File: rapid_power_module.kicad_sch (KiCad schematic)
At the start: 198 parts, among them J1 Conn_02x04_Top_Bottom, J11 SWD Header, J12 SWD Header, J16 USB_C_Receptacle_USB2.0, J17 TC2050, J2 Conn_02x03_Odd_Even, J3 Conn_02x04_Top_Bottom, J4 Conn_02x03_Odd_Even, J5 Molex MicroFit 2x2, J6 Molex MicroFit 2x2, J7 Molex MicroFit 2x2, J8 Molex MicroFit 2x2, J9 Molex MicroFit 2x2, Q1 Q_PMOS, Q2 Q_PMOS, Q3 Q_PMOS, Q4 Q_PMOS, Q5 NMOS, Q6 NMOS, Q7 NMOS, Q8 NMOS, SW1 KMR721NGLFS, SW2 KMR721NGLFS, U1 BQ25756RRVR, U10 L7805, U11 MCP2562-E-SN, U12 STM32F105RCTx, U13 AZ1117I-3.3, U14 TPD4E1U06, U15 TPD4E1U06, U2 CYPD3177-24LQ, U3 BQ76952PFBR, Y3 8MHz 12pF

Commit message: Added Footprints for MOSFETs
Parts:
- J2, J4: footprint (none) -> Connector_PinHeader_2.54mm:PinHeader_2x03_P2.54mm_Vertical
- Q1, Q2, Q3, Q4: footprint (none) -> Package_SO:Diodes_SO-8EP; LCSC (none) -> C531177
- Q5, Q6, Q7, Q8: footprint Package_DFN_QFN:AO_DFN-8-1EP_5.55x5.2mm_P1.27mm_EP4.12x4.6mm -> Package_SON:Infineon_PG-TDSON-8_6.15x5.15mm; LCSC C20266282 -> C501503
- R1: footprint (none) -> Resistor_SMD:R_0402_1005Metric
- TP1: footprint (none) -> TestPoint:TestPoint_Pad_D1.0mm
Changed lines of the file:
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@@
 			)
 		)
-		(property "Footprint" ""
+		(property "Footprint" "Connector_PinHeader_2.54mm:PinHeader_2x03_P2.54mm_Vertical"
 			(at 198.12 161.29 0)
 			(effects
@@
 			)
 		)
-		(property "Footprint" ""
+		(property "Footprint" "Resistor_SMD:R_0402_1005Metric"
 			(at 52.578 54.61 90)
 			(effects
@@
 			)
 		)
-		(property "Footprint" ""
+		(property "Footprint" "Package_SO:Diodes_SO-8EP"
 			(at 349.25 246.38 0)
 			(effects
@@
 			)
 		)
+		(property "LCSC" "C531177"
+			(at 351.79 251.46 90)
+			(effects
+				(font
+					(size 1.27 1.27)
+				)
+				(hide yes)
+			)
+		)
 		(pin "D"
 		)
@@
 			)
 		)
-		(property "Footprint" "Package_DFN_QFN:AO_DFN-8-1EP_5.55x5.2mm_P1.27mm_EP4.12x4.6mm"
+		(property "Footprint" "Package_SON:Infineon_PG-TDSON-8_6.15x5.15mm"
 			(at 134.62 81.28 0)
 			(effects
@@
 			)
 		)
-		(property "LCSC" "C20266282"
+		(property "LCSC" "C501503"
 			(at 139.7 83.82 0)
 			(effects
@@
 			)
 		)
-		(property "Footprint" ""
+		(property "Footprint" "TestPoint:TestPoint_Pad_D1.0mm"
 			(at 283.21 71.12 0)
 			(effects
@@
 			)
 		)
-		(property "Footprint" ""
+		(property "Footprint" "Package_SO:Diodes_SO-8EP"
 			(at 383.54 273.05 0)
 			(effects
@@
 			)
 		)
+		(property "LCSC" "C531177"
+			(at 381 278.13 90)
+			(effects
+				(font
+					(size 1.27 1.27)
+				)
+				(hide yes)
+			)
+		)
 		(pin "S"
 		)
@@
 			)
 		)
-		(property "Footprint" "Package_DFN_QFN:AO_DFN-8-1EP_5.55x5.2mm_P1.27mm_EP4.12x4.6mm"
+		(property "Footprint" "Package_SON:Infineon_PG-TDSON-8_6.15x5.15mm"
 			(at 119.38 81.28 0)
 			(effects
@@
 			)
 		)
-		(property "LCSC" "C20266282"
+		(property "LCSC" "C501503"
 			(at 114.3 83.82 0)
 			(effects
@@
 			)
 		)
-		(property "Footprint" ""
+		(property "Footprint" "Package_SO:Diodes_SO-8EP"
 			(at 349.25 273.05 0)
 			(effects
@@
 			)
 		)
+		(property "LCSC" "C531177"
+			(at 351.79 278.13 90)
+			(effects
+				(font
+					(size 1.27 1.27)
+				)
+				(hide yes)
+			)
+		)
 		(pin "D"
 		)
@@
 			)
 		)
-		(property "Footprint" "Package_DFN_QFN:AO_DFN-8-1EP_5.55x5.2mm_P1.27mm_EP4.12x4.6mm"
+		(property "Footprint" "Package_SON:Infineon_PG-TDSON-8_6.15x5.15mm"
 			(at 134.62 92.71 0)
 			(effects
@@
 			)
 		)
-		(property "LCSC" "C20266282"
+		(property "LCSC" "C501503"
 			(at 139.7 95.25 0)
 			(effects
@@
 			)
 		)
-		(property "Footprint" "Package_DFN_QFN:AO_DFN-8-1EP_5.55x5.2mm_P1.27mm_EP4.12x4.6mm"
+		(property "Footprint" "Package_SON:Infineon_PG-TDSON-8_6.15x5.15mm"
 			(at 119.38 92.71 0)
 			(effects
@@
 			)
 		)
-		(property "LCSC" "C20266282"
+		(property "LCSC" "C501503"
 			(at 114.3 95.25 0)
 			(effects
@@
 			)
 		)
-		(property "Footprint" ""
+		(property "Footprint" "Package_SO:Diodes_SO-8EP"
 			(at 383.54 246.38 0)
 			(effects
@@
 			)
 		)
+		(property "LCSC" "C531177"
+			(at 381 251.46 90)
+			(effects
+				(font
+					(size 1.27 1.27)
+				)
+				(hide yes)
+			)
+		)
 		(pin "S"
 		)
@@
 			)
 		)
-		(property "Footprint" ""
+		(property "Footprint" "Connector_PinHeader_2.54mm:PinHeader_2x03_P2.54mm_Vertical"
 			(at 179.07 161.29 0)
 			(effects

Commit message: Further Routing work and fixed the Q Pins
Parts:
- removed Q1, Q2, Q3, Q4: Q_PMOS, Package_SO:Diodes_SO-8EP, symbol Device:Q_PMOS
- added Q1, Q12, Q2, Q3: AOSP21321, Package_SO:SO-8_3.9x4.9mm_P1.27mm, symbol euroc_fc:AOSP21321
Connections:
- net SAFE_PWR_OUT: now also Q3.1 (S), Q3.2 (S), Q3.3 (S)
- net USB_PD_OUT: now also Q1.1 (S), Q1.2 (S), Q1.3 (S)
- net VBUS: now also Q12.5 (D), Q12.6 (D), Q12.7 (D), Q12.8 (D), Q2.5 (D), Q2.6 (D), Q2.7 (D), Q2.8 (D)
- net at C10.2, C9.2, R4.2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: now also Q1.4 (G), Q12.4 (G)
- net at R8.2, R9.1: now also Q2.4 (G), Q3.4 (G)
- new net: Q1.5 (D), Q1.6 (D), Q1.7 (D), Q1.8 (D), Q12.1 (S), Q12.2 (S), Q12.3 (S)
- new net: Q2.1 (S), Q2.2 (S), Q2.3 (S), Q3.5 (D), Q3.6 (D), Q3.7 (D), Q3.8 (D)

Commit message: Further Routing work and fixed the Q Pins
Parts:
- removed Q5, Q6, Q7, Q8: NMOS, Package_SON:Infineon_PG-TDSON-8_6.15x5.15mm, symbol Simulation_SPICE:NMOS
- added Q4: HiDRV1, Package_TO_SOT_SMD:TDSON-8-1, symbol Transistor_FET:BSC070N10NS5
- added Q5: LoDRV1, Package_TO_SOT_SMD:TDSON-8-1, symbol Transistor_FET:BSC070N10NS5
- added Q6: HiDRV2, Package_TO_SOT_SMD:TDSON-8-1, symbol Transistor_FET:BSC070N10NS5
- added Q7: LoDRV2, Package_TO_SOT_SMD:TDSON-8-1, symbol Transistor_FET:BSC070N10NS5
- added R25: 20k, Resistor_SMD:R_0402_1005Metric, symbol Device:R
- added R27: 50k, Resistor_SMD:R_0402_1005Metric, symbol Device:R
- R83: footprint Resistor_SMD:R_0603_1608Metric -> Resistor_SMD:R_0402_1005Metric; LCSC (none) -> C23184
- R94: value 16k -> 20k; footprint Resistor_SMD:R_0603_1608Metric -> Resistor_SMD:R_0402_1005Metric; LCSC (none) -> C25765
- R95: value 8k -> 10k; footprint Resistor_SMD:R_0603_1608Metric -> Resistor_SMD:R_0402_1005Metric; LCSC (none) -> C25744
- R96: value 4k -> 5.1k; footprint Resistor_SMD:R_0603_1608Metric -> Resistor_SMD:R_0402_1005Metric; LCSC (none) -> C25905
- R97: footprint Resistor_SMD:R_0603_1608Metric -> Resistor_SMD:R_0402_1005Metric; LCSC (none) -> C25765
- R98: value 12.5k -> 15k; LCSC (none) -> C25756
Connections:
- net BuckBoostOut: now also Q6.5 (D)
- net HIDRV1: now also Q4.4 (G)
- net HIDRV2: now also Q6.4 (G)
- net LODRV1: now also Q5.4 (G)
- net LODRV2: now also Q7.4 (G)
- net PACK+: now also BT1.P (+); no longer BT1.1 (+)
- net PGND: now also BT3.N (-), Q5.1 (S), Q5.2 (S), Q5.3 (S), Q7.1 (S), Q7.2 (S), Q7.3 (S), R25.2, R27.2; no longer BT3.2 (-)
- net SW1: now also Q4.1 (S), Q4.2 (S), Q4.3 (S), Q5.5 (D)
- net SW2: now also Q6.1 (S), Q6.2 (S), Q6.3 (S), Q7.5 (D)
- net at J4.1 (Pin_1): now also R27.1
- net at C4.1, C7.1, R65.2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: now also Q4.5 (D)
- net at J2.1 (Pin_1): now also R25.1
- new net: BT2.N (-), BT3.P (+), R12.1
- new net: BT1.N (-), BT2.P (+), R11.1
- no-connect marks 40 -> 38
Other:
- note removed: "TODO: Set Values"
- moved on the sheet: J2, J4, R32, R36, R82, R94, R95, R96, R97, R98, TH1

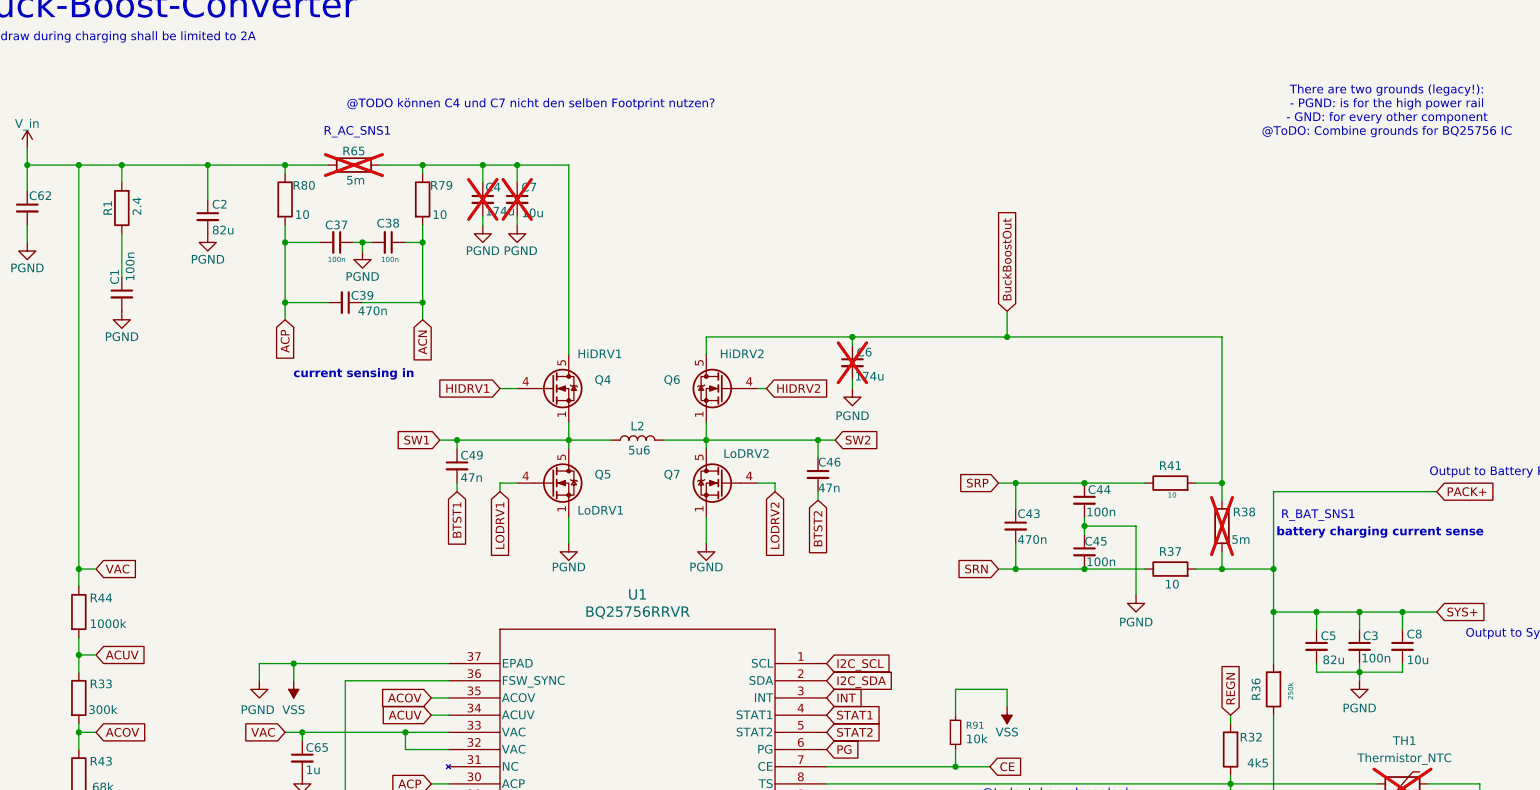
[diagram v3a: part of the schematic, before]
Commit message: Fixed wuerth cap footprints and values
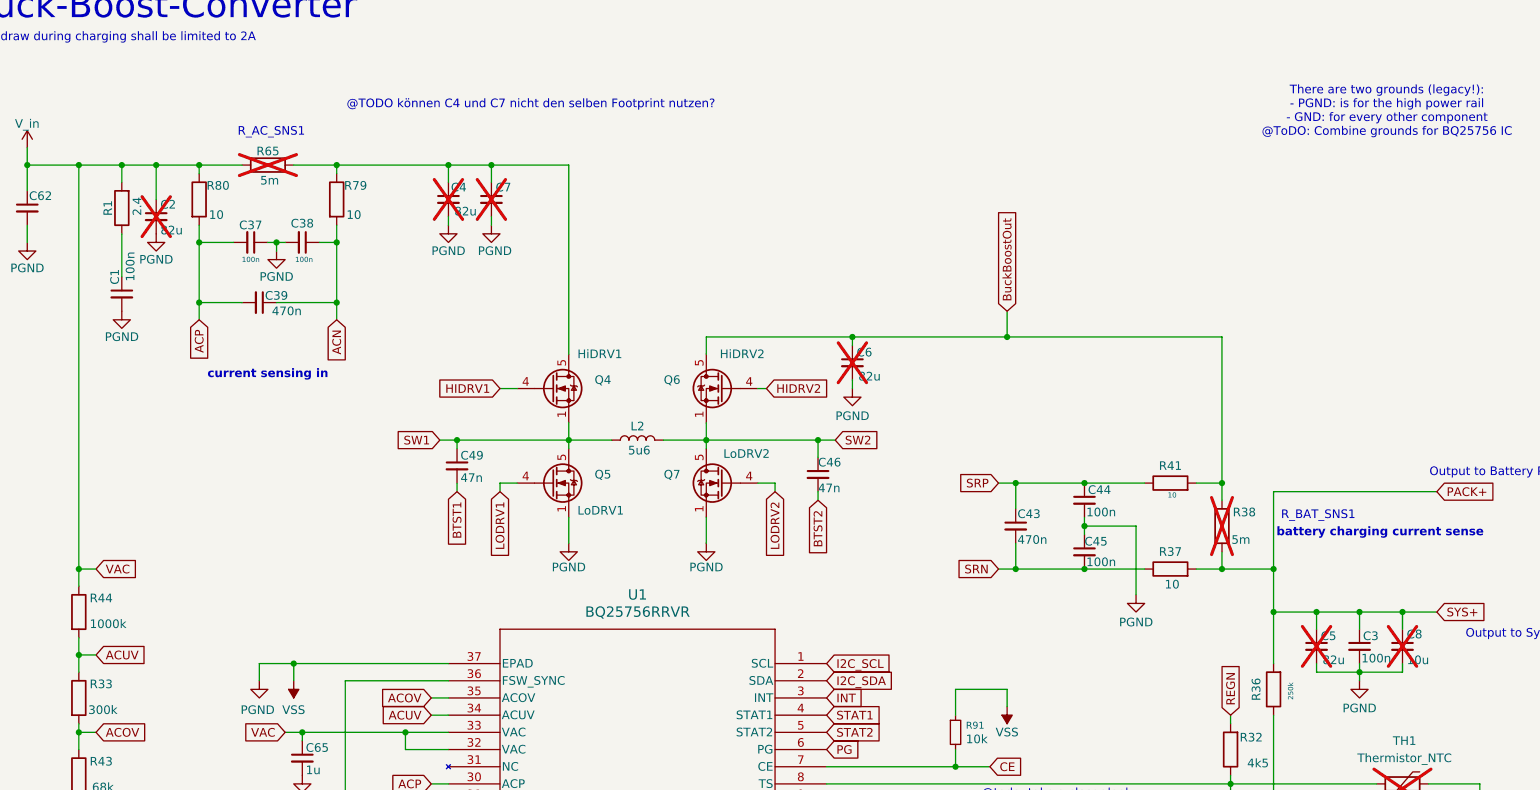
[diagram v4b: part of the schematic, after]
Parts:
- C2, C5: footprint Capacitor_SMD:C_0603_1608Metric -> Capacitor_SMD:CP_Elec_8x6.9; now not fitted
- C4, C6: value 174u -> 82u
- C8: footprint Capacitor_SMD:C_0603_1608Metric -> Capacitor_SMD:CP_Elec_6.3x5.9; now not fitted
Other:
- moved on the sheet: C37, C38, C39, C4, C7, R65, R79, R80

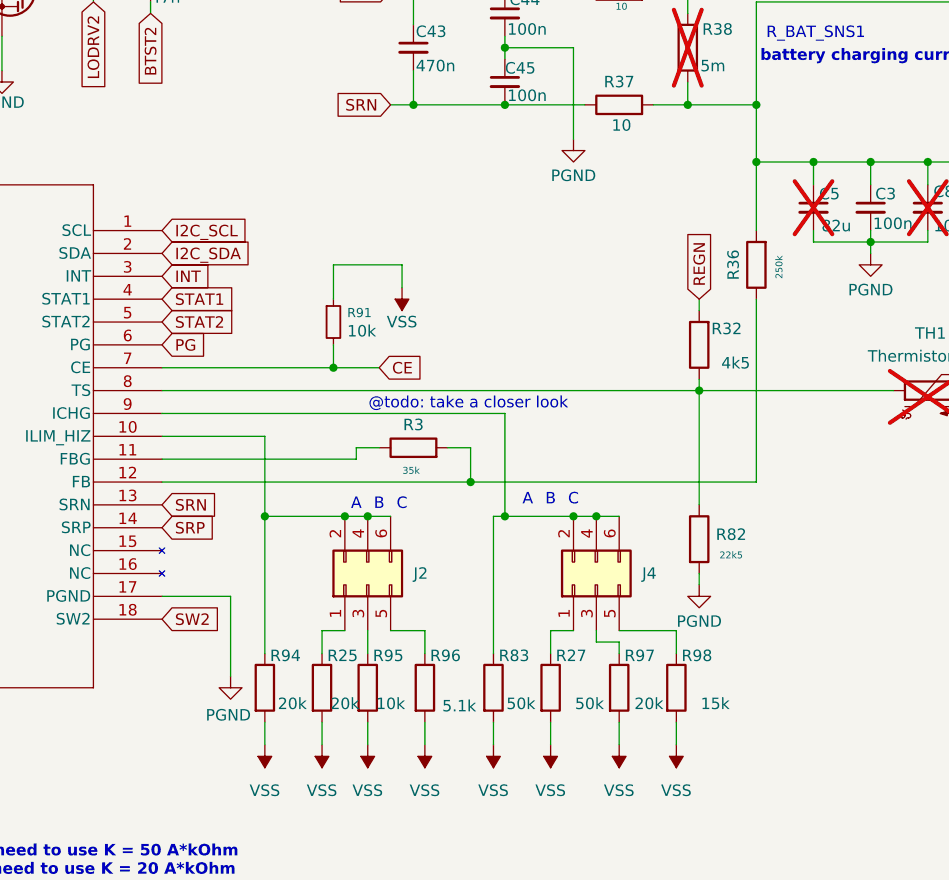
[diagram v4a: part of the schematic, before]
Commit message: Added footprints and LCSC
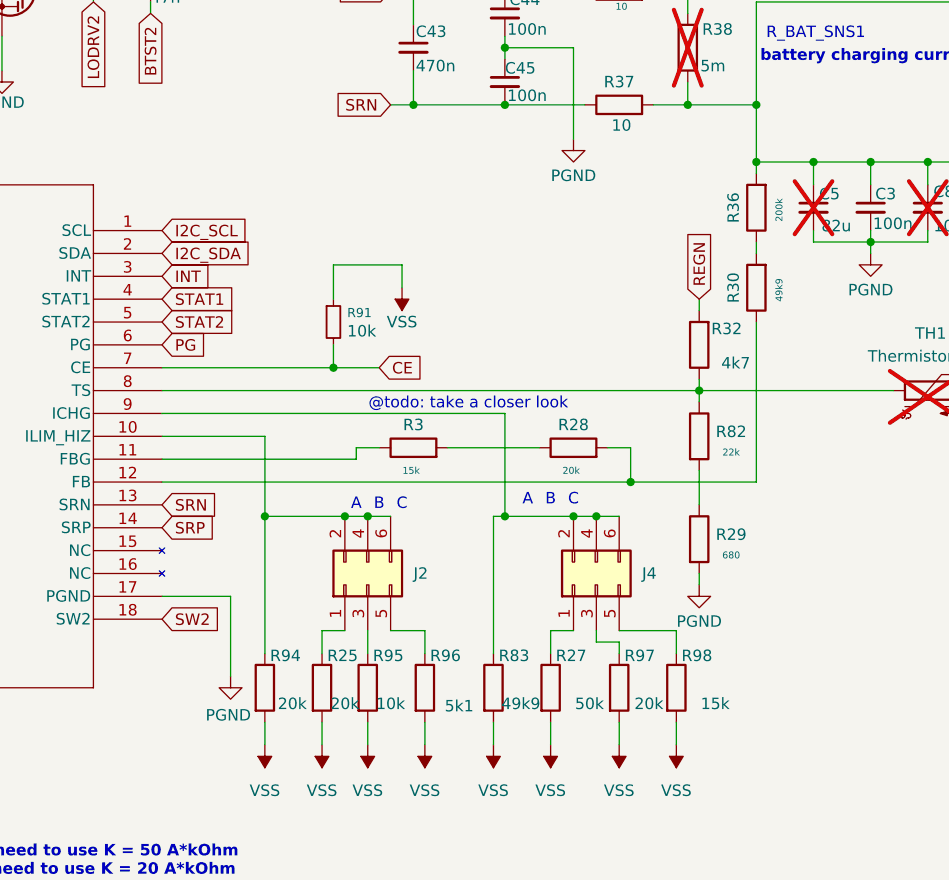
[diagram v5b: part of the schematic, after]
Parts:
- added R28: 20k, Resistor_SMD:R_0603_1608Metric, symbol Device:R
- added R29: 680, Resistor_SMD:R_0603_1608Metric, symbol Device:R
- added R30: 49k9, Resistor_SMD:R_0603_1608Metric, symbol Device:R
- C14, C15, C16, C17: LCSC (none) -> C21120
- C21: LCSC (none) -> C377773
- R11, R12, R2, R20: footprint Resistor_SMD:R_2512_6332Metric -> Resistor_SMD:R_1206_3216Metric; LCSC (none) -> C17955
- R23: LCSC (none) -> C25900
- R24: LCSC (none) -> C25741
- R3: value 35k -> 15k; LCSC (none) -> C25756
- R32: value 4k5 -> 4k7; LCSC (none) -> C25900
- R33: LCSC (none) -> C23024
- R36: value 250k -> 200k; LCSC (none) -> C25764
- R37, R41, R79, R80: LCSC (none) -> C25077
- R4: LSC (none) -> C25744
- R8: LCSC (none) -> C23184
- R82: value 22k5 -> 22k; LCSC (none) -> C25768
- R83: value 50k -> 49k9
- R91: LCSC (none) -> C25744
- R96: value 5.1k -> 5k1
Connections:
- net PGND: now also R29.2; no longer R82.2
- new net: R28.2, R30.1, U1.12 (FB)
- new net: R29.1, R82.2
- new net: R30.2, R36.1
- new net: R28.1, R3.2
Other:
- moved on the sheet: R36, R82

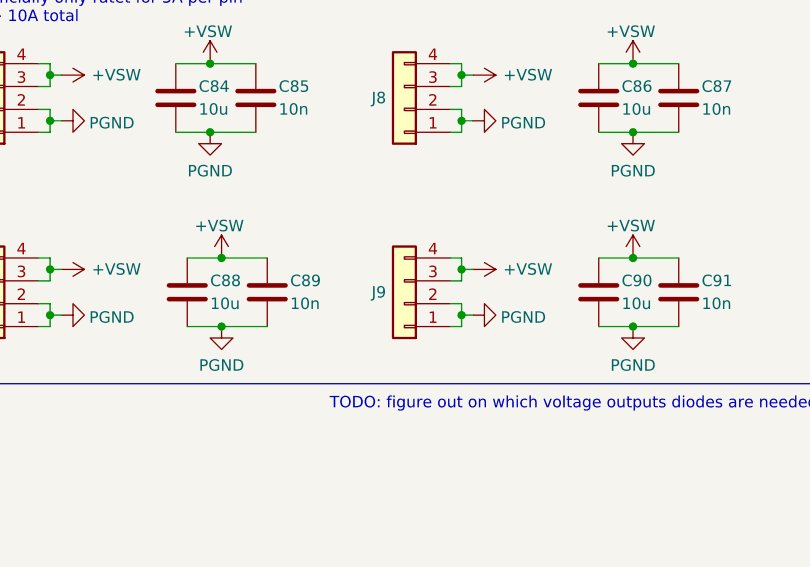
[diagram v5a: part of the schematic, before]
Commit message: Added Diode and new connector type
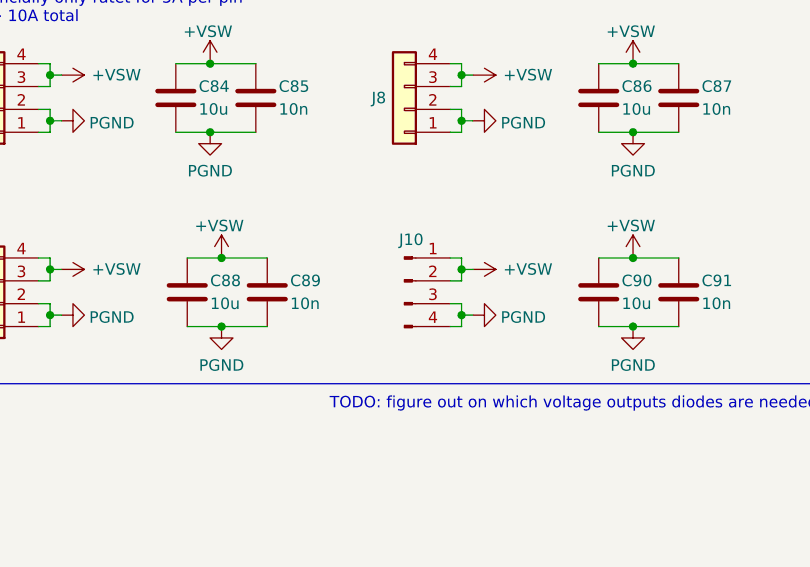
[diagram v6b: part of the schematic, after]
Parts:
- removed J9: Molex MicroFit 2x2, Connector_Molex:Molex_Micro-Fit_3.0_43045-0400_2x02_P3.00mm_Horizontal, symbol Connector_Generic:Conn_01x04
- added J10: JST-GH 4Pin, Connector_JST:JST_GH_SM04B-GHS-TB_1x04-1MP_P1.25mm_Horizontal, symbol Connector:Conn_01x04_Pin
- C1, C37, C38: footprint Capacitor_SMD:C_0603_1608Metric -> Capacitor_SMD:C_0402_1005Metric; LCSC C14663 -> C307331
- C11: LCSC (none) -> C52923
- C12, C13: LCSC (none) -> C307331
- C18: LCSC (none) -> C1623
- C3, C44, C45: footprint Capacitor_SMD:C_0603_1608Metric -> Capacitor_SMD:C_0402_1005Metric; LCSC (none) -> C307331
- C46, C49: LCSC (none) -> C1622
- C59, C69, C70, C71, C72: LCSC# C77020 -> C307331
- C60: footprint Capacitor_SMD:C_0603_1608Metric -> Capacitor_SMD:C_0402_1005Metric; LCSC# C14663 -> C307331
- C68, C81: LCSC (none) -> C307331; LCSC# C77020 -> (none)
- C79: LCSC C1525 -> C307331
- C82, C84, C88: LCSC (none) -> C194427; LCSC# C194427 -> (none)
- C83, C85, C89: LCSC (none) -> C60133; LCSC# C60133 -> (none)
- D4: footprint Diode_SMD:ST_D_SMC -> Package_TO_SOT_THT:TO-220-3_Vertical; LCSC C31849 -> C5358933
- R22: LCSC (none) -> C25077
- R35: footprint Resistor_SMD:R_0603_1608Metric -> Capacitor_SMD:C_0402_1005Metric; LCSC (none) -> C25079
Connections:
- net +VSW: now also J10.1 (Pin_1), J10.2 (Pin_2)
- net PGND: now also J10.3 (Pin_3), J10.4 (Pin_4)
